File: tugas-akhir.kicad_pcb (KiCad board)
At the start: 2 copper layers, 155 x 75.5 mm, 34 parts, among them J1 Conn_01x02_Socket, J2 Conn_01x02_Pin (solenoid lini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, K1 Relay_SPDT, M1 Stepper_Motor_bipolar / Nema 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, M2 Stepper_Motor_bipolar / Nema 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, M3 Stepper_Motor_bipolar / Nema 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, Q1 2N3904, U1 ESP32-DEVKIT-V1, U2 DCDC_StepDown_LM2596, U3 TMC2208_SILENTSTEPSTICK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

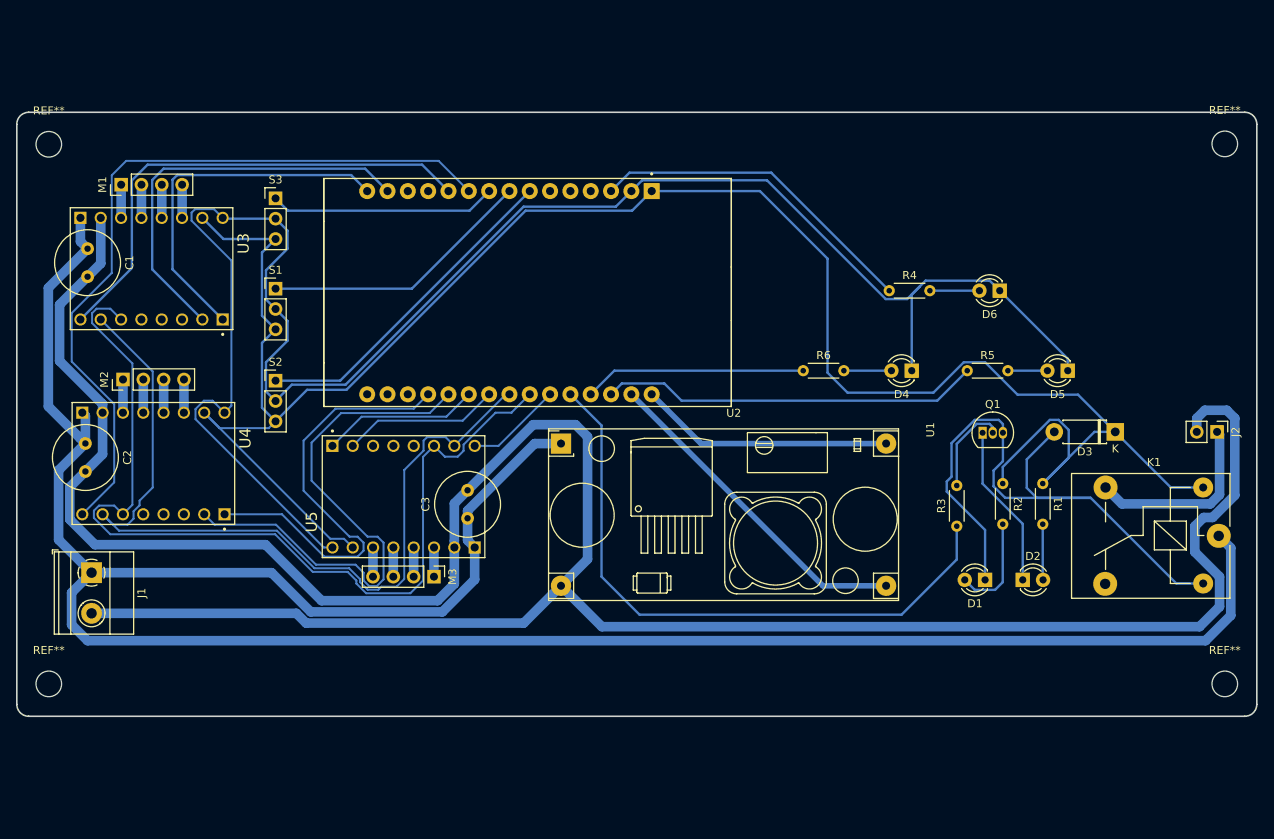
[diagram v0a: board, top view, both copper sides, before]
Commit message: new pcb route
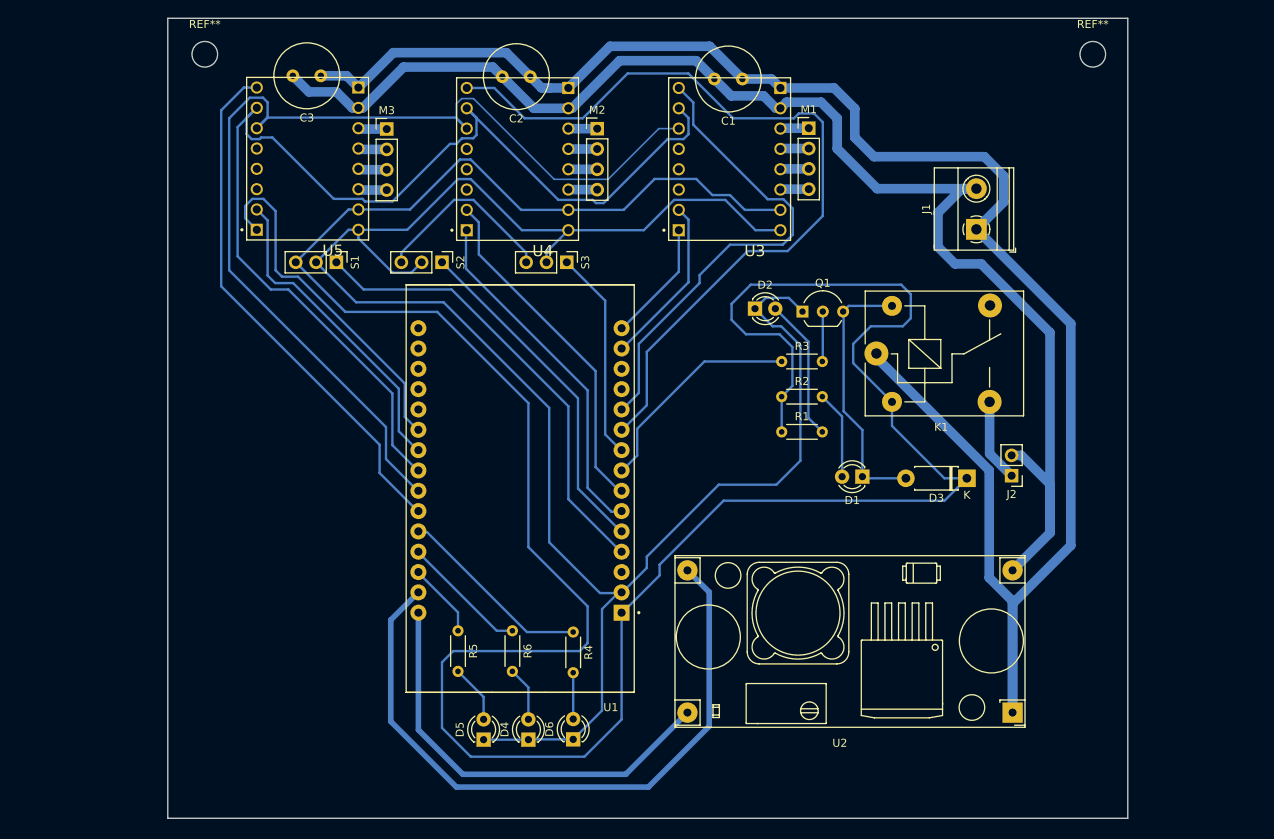
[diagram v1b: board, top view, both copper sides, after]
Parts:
- removed the REF** at (69.0, 125.2)
- removed the REF** at (216.0, 57.7)
- removed the REF** at (69.0, 57.8)
- removed the REF** at (216.0, 125.2)
- added REF**: MountingHole_3.2mm_M3_ISO14580, MountingHole:MountingHole_3.2mm_M3_ISO14580, F.Cu at (88.5, 46.5)
- added REF**: MountingHole_3.2mm_M3_ISO14580, MountingHole:MountingHole_3.2mm_M3_ISO14580, F.Cu at (199.5, 46.5)
- Q1: footprint Package_TO_SOT_THT:TO-92_Inline -> Package_TO_SOT_THT:TO-92_Inline_Wide
- moved J1 118.6 mm to (184.9, 68.4), turned to 90 degrees
- moved D5 86.4 mm to (123.3, 132.2), turned to 90 degrees
- moved M1 86.2 mm to (164.0, 55.7), turned to 0 degrees
- moved C1 84.6 mm to (155.7, 49.6), turned to 180 degrees
- moved D6 77.4 mm to (134.6, 132.1), turned to 90 degrees
- moved U3 73.5 mm to (154.1, 59.6), turned to 180 degrees
- moved C2 72.1 mm to (129.2, 49.3), turned to 180 degrees
- moved R5 71.5 mm to (120.2, 118.6), turned to -90 degrees
- moved M2 67.1 mm to (137.6, 55.8), turned to 0 degrees
- moved D4 66.5 mm to (128.9, 132.2), turned to 90 degrees
- moved U2 65.7 mm to (189.5, 128.8), turned to 180 degrees
- moved U4 59.3 mm to (127.6, 59.6), turned to 180 degrees
- moved C3 58.3 mm to (103.0, 49.2), turned to 180 degrees
- moved R4 58.2 mm to (134.6, 118.7), turned to -90 degrees
- moved M3 56.3 mm to (111.2, 55.9), turned to 0 degrees
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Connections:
- R3 pad 1: Net-(U1-D14) -> Net-(U1-D5)
- R4 pad 1: Net-(U1-D15) -> Net-(U1-D14)
- S1 pad 1: Net-(U1-D5) -> Net-(U1-D2)
- S2 pad 1: Net-(U1-TX2) -> Net-(U1-D4)
- U1 pad 19: Net-(U1-D34) -> unconnected-(U1-D34-Pad19)
- U1 pad 20: Net-(U1-D35) -> unconnected-(U1-D35-Pad20)
- U1 pad 3: Net-(U1-D15) -> unconnected-(U1-D15-Pad3)
- U1 pad 4: unconnected-(U1-D2-Pad4) -> Net-(U1-D2)
- U1 pad 5: unconnected-(U1-D4-Pad5) -> Net-(U1-D4)
- U1 pad 6: unconnected-(U1-RX2-Pad6) -> Net-(U1-RX2)
- U4 pad JP1_1: Net-(U1-D34) -> Net-(U1-RX2)
- U4 pad JP1_2: Net-(U1-D35) -> Net-(U1-TX2)
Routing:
- net -24V: track 329.8 -> 176.1 mm
- net Net-(D3-K): track 259.2 -> 364.1 mm
- net Net-(U1-D35): track 68.2 -> 0.00 mm
- net +24V: track 296.6 -> 228.9 mm
- net Net-(U1-D2): track 0.00 -> 57.5 mm
- net Net-(U1-D34): track 55.3 -> 0.00 mm
- net Net-(U1-D27): track 12.1 -> 66.0 mm
- net Net-(U1-D14): track 77.8 -> 24.5 mm
- net Net-(D1-K): track 83.6 -> 33.6 mm
- net Net-(U1-RX2): track 0.00 -> 44.0 mm
- net Net-(U1-D4): track 0.00 -> 43.0 mm
- net Net-(U1-GND-Pad29): track 41.8 -> 84.5 mm
- net Net-(U1-D15): track 41.8 -> 0.00 mm
- net Net-(U1-D13): track 47.5 -> 9.30 mm
- net Net-(U1-D25): track 108.0 -> 140.5 mm
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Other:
- board size 155 x 75.5 mm -> 120 x 100 mm

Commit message: finish pcb route
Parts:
- added REF**: MountingHole_3.2mm_M3_ISO14580, MountingHole:MountingHole_3.2mm_M3_ISO14580, F.Cu at (200.2, 138.6)
- added REF**: MountingHole_3.2mm_M3_ISO14580, MountingHole:MountingHole_3.2mm_M3_ISO14580, F.Cu at (88.2, 138.6)
- moved REF** 0.71 mm to (200.2, 46.6)
- moved D6 0.50 mm to (134.7, 132.6)
- moved U2 0.50 mm to (189.6, 129.3)
- moved C1 0.50 mm to (155.8, 50.1)
- moved C2 0.50 mm to (129.3, 49.8)
- moved C3 0.50 mm to (103.1, 49.7)
- moved D1 0.50 mm to (170.8, 99.8)
- moved D2 0.50 mm to (157.4, 78.8)
- moved D3 0.50 mm to (183.9, 100.0)
- moved J1 0.50 mm to (185.1, 68.9)
- moved J2 0.50 mm to (189.5, 99.7)
- moved K1 0.50 mm to (172.6, 84.4)
- moved M1 0.50 mm to (164.1, 56.2)
- moved M2 0.50 mm to (137.7, 56.3)
- moved M3 0.50 mm to (111.4, 56.3)
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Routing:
- net Net-(D3-K): track 364.1 -> 357.2 mm
- net Net-(D2-K): track 241.3 -> 238.7 mm
- net Net-(U1-D25): track 140.5 -> 139.0 mm
- net Net-(U1-D33): track 39.9 -> 38.5 mm
- net +24V: track 228.9 -> 229.7 mm
- net Net-(U1-D27): track 66.0 -> 66.8 mm
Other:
- outline, holes or cut-outs redrawn
- board text added: "+ -"
- board text added: "24V"
- board text added: "DC Step Down"
- board text added: "ESP32 DEVKIT V1"
- board text added: "IoT-LD-I131 TA-NANANG"
- board text added: "Relay"
- board text added: "TMC2208 X"
- board text added: "TMC2208 Z"
- board text added: "TMC2208 Z'"
- board text added: "x z' z"

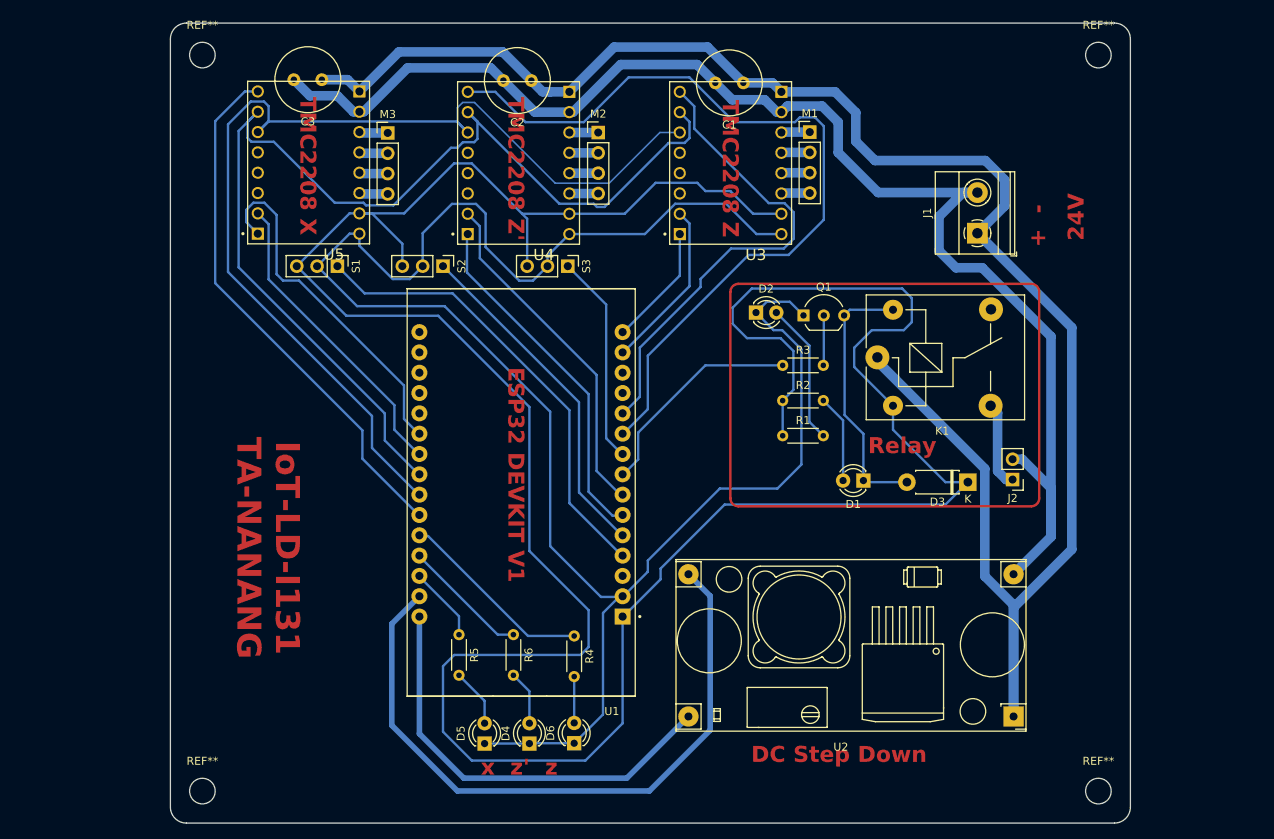
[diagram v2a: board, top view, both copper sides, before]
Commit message: change size of resistor and terminal block
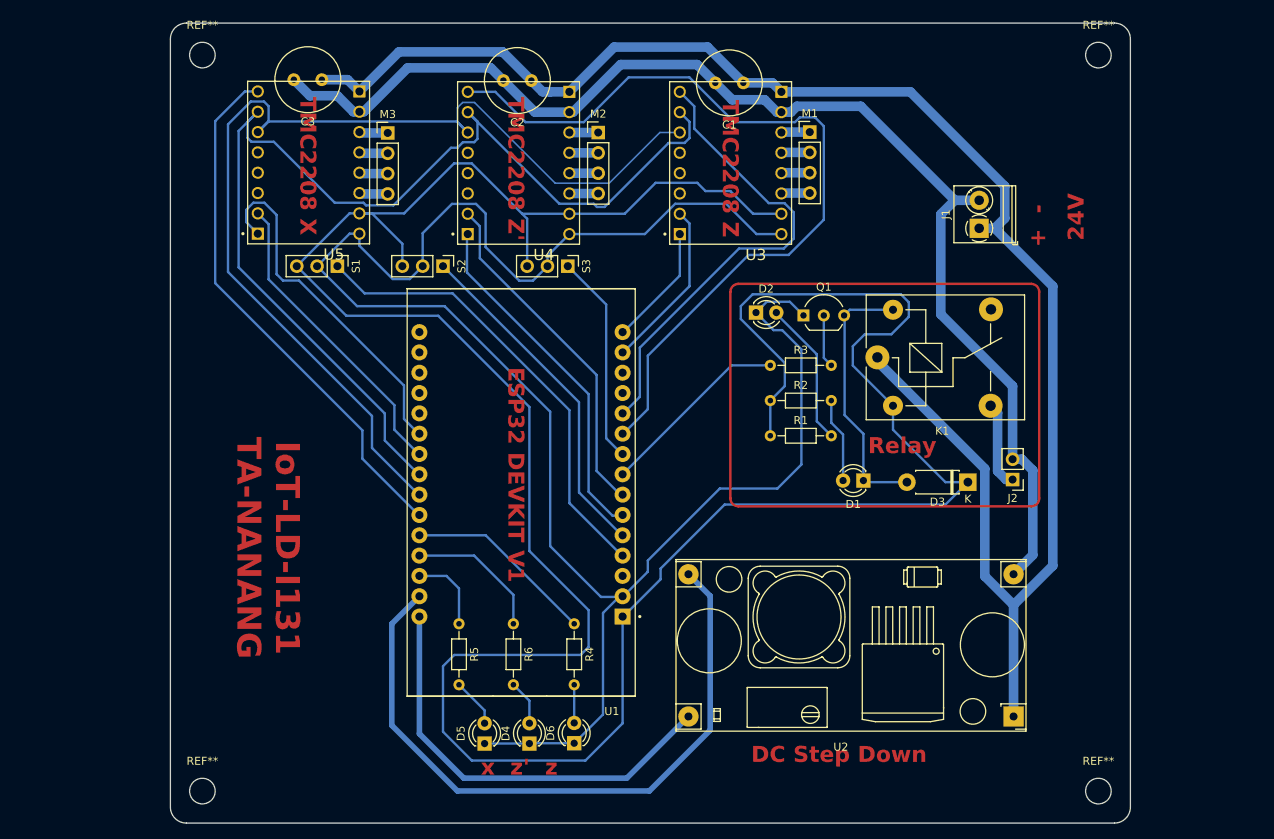
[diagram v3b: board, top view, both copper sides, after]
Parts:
- J1: footprint TerminalBlock_Phoenix:TerminalBlock_Phoenix_MKDS-1,5-2-5.08_1x02_P5.08mm_Horizontal -> TerminalBlock_Phoenix:TerminalBlock_Phoenix_PT-1,5-2-3.5-H_1x02_P3.50mm_Horizontal
- R1, R2, R3, R4, R5, R6: footprint Resistor_THT:R_Axial_DIN0204_L3.6mm_D1.6mm_P5.08mm_Horizontal -> Resistor_THT:R_Axial_DIN0204_L3.6mm_D1.6mm_P7.62mm_Horizontal
- moved R1 1.55 mm to (159.2, 94.2)
- moved R2 1.55 mm to (159.2, 89.8)
- moved R3 1.55 mm to (159.2, 85.4)
- moved R4 1.52 mm to (134.7, 117.7)
- moved R5 1.36 mm to (120.3, 117.7)
- moved R6 1.36 mm to (127.1, 117.7)
- moved J1 0.65 mm to (185.3, 68.2)
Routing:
- net -24V: track 176.4 -> 155.9 mm
- net +24V: track 229.7 -> 211.4 mm
- net Net-(D3-K): track 357.2 -> 351.4 mm
- net Net-(U1-D5): track 27.7 -> 24.1 mm
- net Net-(U1-D12): track 15.8 -> 17.4 mm
- net Net-(D4-A): track 6.82 -> 5.64 mm
- net Net-(D5-A): track 7.32 -> 6.14 mm
- net Net-(D6-A): track 5.80 -> 4.77 mm
- net Net-(U1-D13): track 9.30 -> 10.0 mm
- net Net-(U1-D14): track 24.5 -> 23.9 mm
- net Net-(U1-D21): track 60.1 -> 59.5 mm

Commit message: minor revision
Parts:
- C1, C2, C3: footprint Capacitor_THT:C_Radial_D8.0mm_H11.5mm_P3.50mm -> Capacitor_THT:CP_Radial_D8.0mm_P3.50mm
- D3: value D -> 1N4007
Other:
- board text added: "C1"
- board text added: "C2"
- board text added: "C3"
- board text added: "D1"
- board text added: "D2"
- board text added: "D3"
- board text added: "D4"
- board text added: "D5"
- board text added: "D6"
- board text added: "J1"
- board text added: "J2"
- board text added: "MX"
- board text added: "MZ"
- board text added: "MZ'"
- board text added: "Q1"
- board text added: "R1"
- board text added: "R2"
- board text added: "R3"
- board text added: "R4"
- board text added: "R5"
- board text added: "R6"
- board text added: "SX"
- board text added: "SZ"
- board text added: "SZ'"
- board text added: "TMC 2208 X"
- board text added: "TMC 2208 Z"
- board text added: "TMC 2208 Z'"
- board text added: "→"
- board text removed: "TMC2208 X"
- board text removed: "TMC2208 Z"
- board text removed: "TMC2208 Z'"

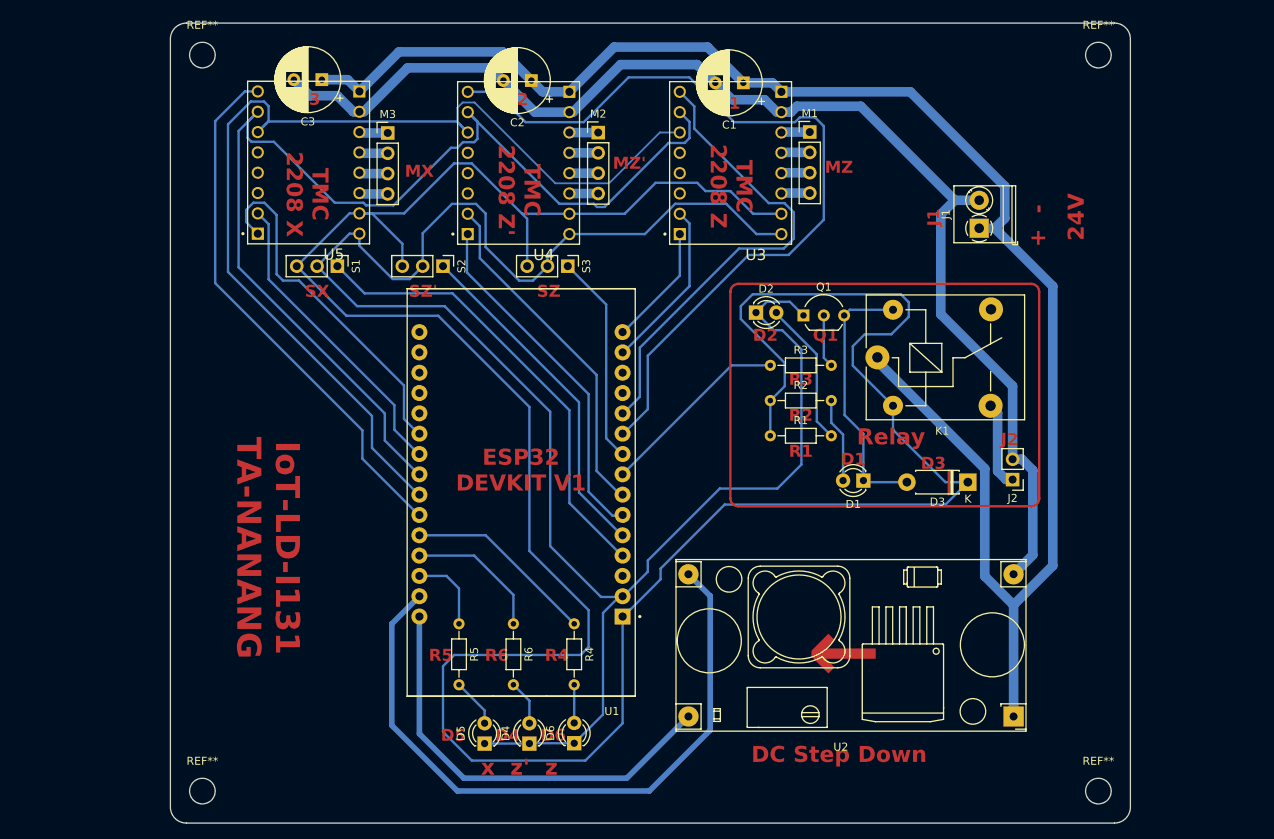
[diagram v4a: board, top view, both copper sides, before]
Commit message: update driver routes
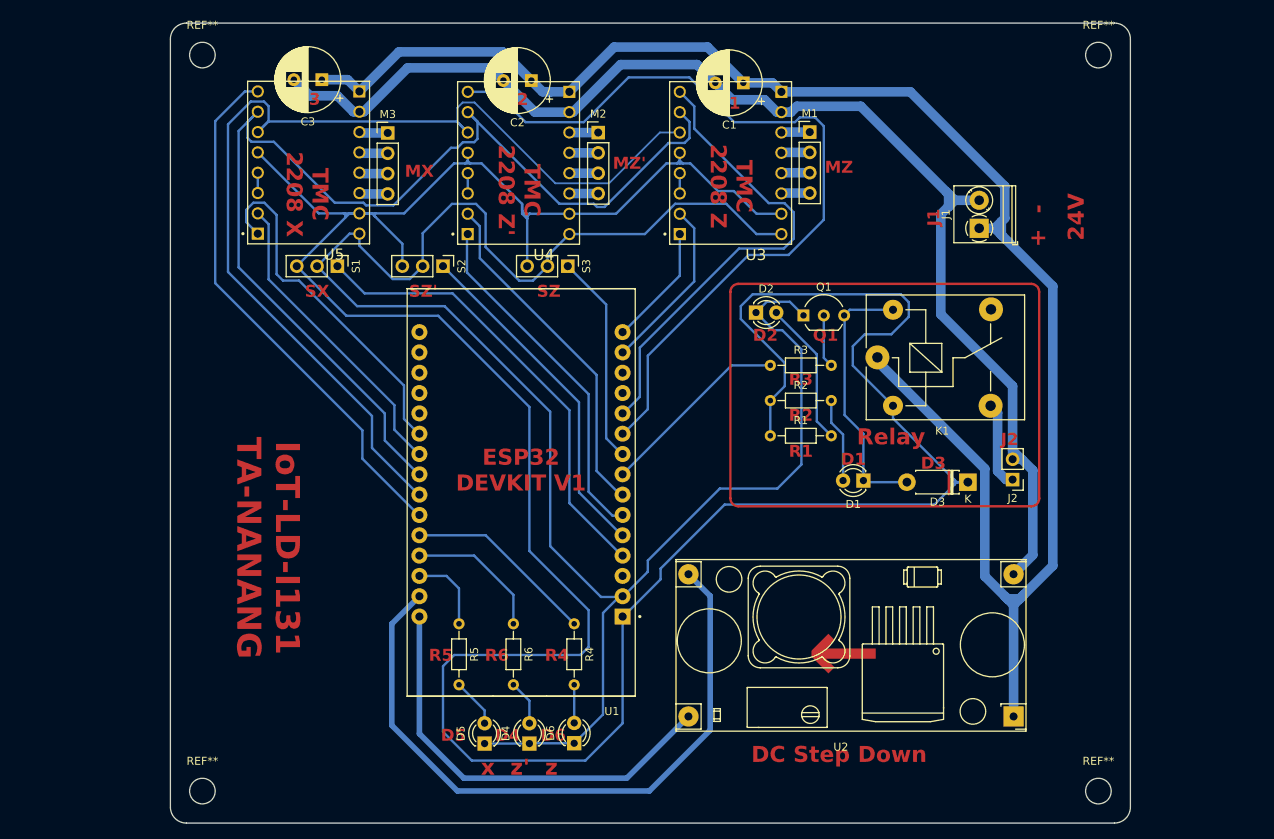
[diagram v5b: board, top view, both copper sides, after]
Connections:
- U3 pad JP1_3: unconnected-(U3-CLK-PadJP1_3) -> Net-(U3-CLK)
- U3 pad JP1_4: unconnected-(U3-PDN/UART1-PadJP1_4) -> Net-(U3-CLK)
- U3 pad JP1_5: unconnected-(U3-NC-PadJP1_5) -> Net-(D3-K)
- U4 pad JP1_3: unconnected-(U4-CLK-PadJP1_3) -> Net-(U4-CLK)
- U4 pad JP1_4: unconnected-(U4-PDN/UART1-PadJP1_4) -> Net-(U4-CLK)
- U4 pad JP1_5: unconnected-(U4-NC-PadJP1_5) -> Net-(D3-K)
- U5 pad JP1_3: unconnected-(U5-CLK-PadJP1_3) -> Net-(U5-CLK)
- U5 pad JP1_4: unconnected-(U5-PDN/UART1-PadJP1_4) -> Net-(U5-CLK)
- U5 pad JP1_5: unconnected-(U5-NC-PadJP1_5) -> Net-(D3-K)
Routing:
- net Net-(D3-K): track 351.4 -> 380.1 mm
- net +24V: track 211.4 -> 215.7 mm
- net -24V: track 155.9 -> 159.5 mm
- net Net-(U4-CLK): track 0.00 -> 2.54 mm
- net Net-(U3-CLK): track 0.00 -> 2.54 mm
- net Net-(U5-CLK): track 0.00 -> 2.54 mm
